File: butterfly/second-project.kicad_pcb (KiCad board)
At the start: 2 copper layers, 85.9 x 65.5 mm, 11 parts, among them SW1 SW_Push

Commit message: added readme
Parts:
- added G***: LOGO, LOGO, F.Cu at (141.5, 138.0)

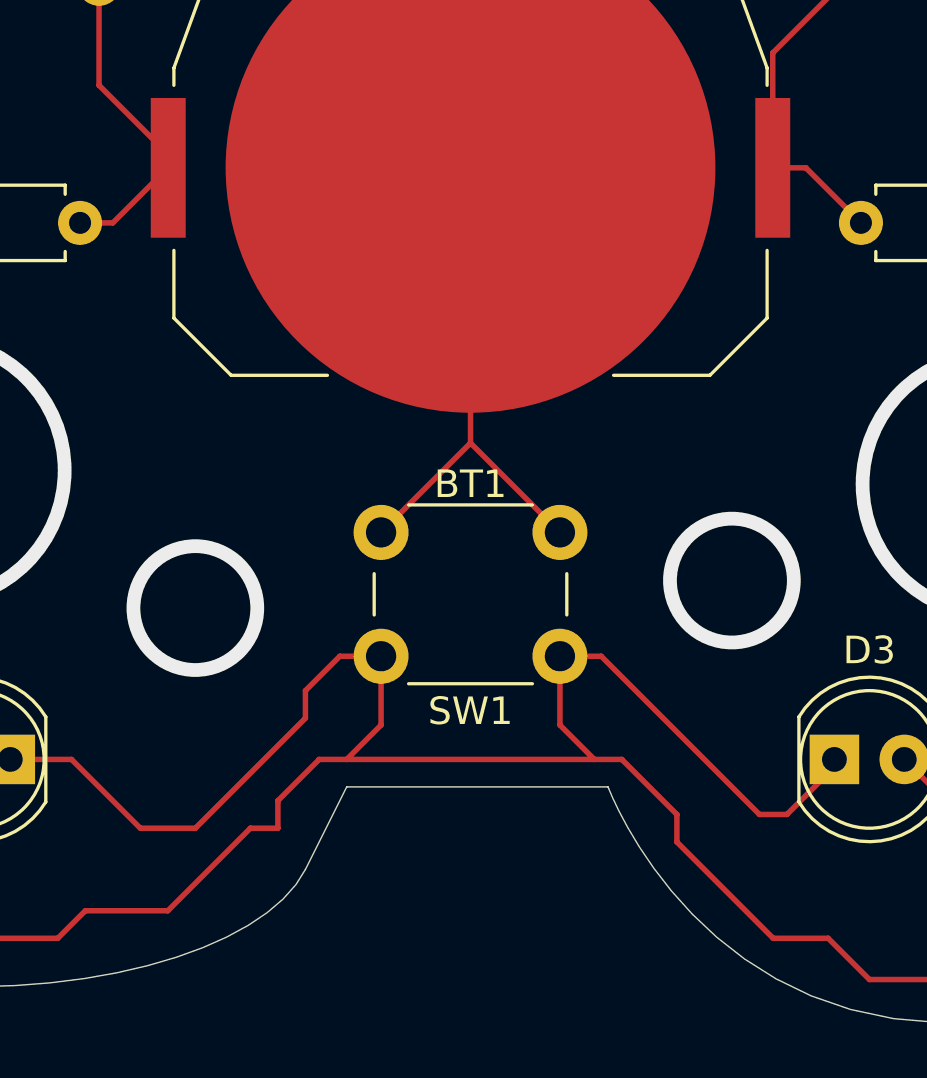
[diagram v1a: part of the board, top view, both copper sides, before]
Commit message: Fixed connection with button
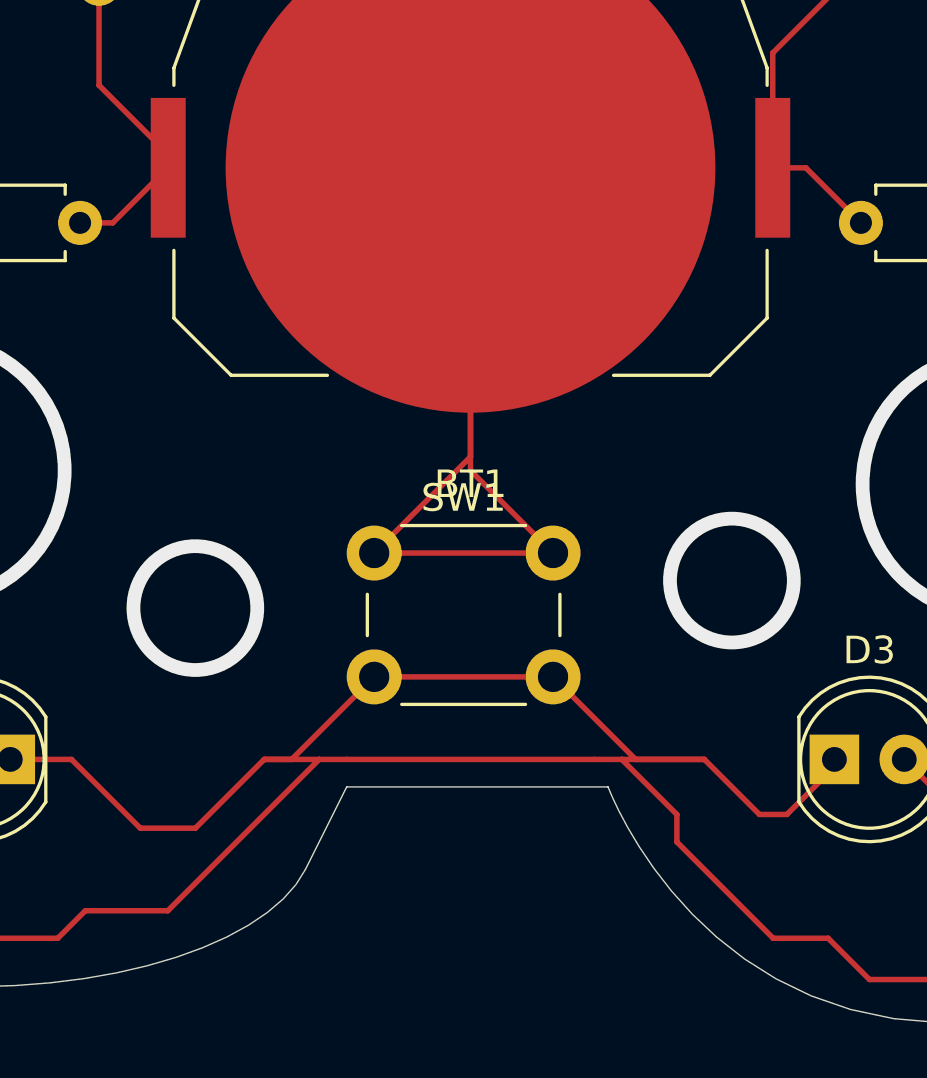
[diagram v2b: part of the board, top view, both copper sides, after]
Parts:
- moved SW1 7.72 mm to (116.5, 132.0), turned to 0 degrees
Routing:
- net Net-(BT1--): track 19.2 -> 37.2 mm, vias 1 -> 2
- net Net-(D1-K): track 188.9 -> 190.1 mm, vias 0 -> 1
- net (no net): vias 6 -> 4
